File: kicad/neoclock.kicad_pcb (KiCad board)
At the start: 2 copper layers, 28.1 x 42.7 mm, 22 parts, among them CON1 2.1mm 5V, IC1 ATMEGA328P-A, K1 NEOPIXEL, P1 ICSP, SW1 HOUR, SW2 MINUTE, U1 DS1307, X1 16Mhz, X2 32.768kHz

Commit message: updated qfn board
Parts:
- added F1: FUSE, synic:1206_polyfuse, F.Cu at (33.0, 51.3)
- added MH: MountingHole_2-5mm_RevA_Date21Jun2010, Mounting_Holes:MountingHole_2-5mm, F.Cu at (72.6, 56.1)
- added MH: MountingHole_2-5mm_RevA_Date21Jun2010, Mounting_Holes:MountingHole_2-5mm, F.Cu at (42.2, 37.8)
- added MH1: MountingHole_2-5mm_RevA_Date21Jun2010, Mounting_Holes:MountingHole_2-5mm, F.Cu at (72.6, 37.8)
- added TP1: TPGND, synicpretty:TESTPOINT, F.Cu at (73.9, 50.8)
- added TP2: TPVCC, TESTPOINT, F.Cu at (73.9, 47.2)
- C4: footprint Capacitors_SMD:c_elec_3x5.3 -> Capacitors_SMD:c_elec_4x5.3
- CON1: footprint synic:BARREL_JACK_SMD -> BARREL_JACK_SMD
- IC1: value ATMEGA328P-A -> ATMEGA328P-MM; footprint SMD_Packages:TQFP32 -> SMD_Packages:QFN28
- PHOTOR1: footprint synic:PHOTORESISTOR -> PHOTORESISTOR
- SW1: value HOUR -> H
- SW2: value MINUTE -> M
- moved U1 45.8 mm to (59.9, 47.0)
- moved X2 43.2 mm to (67.1, 47.8)
- moved C5 40.7 mm to (52.1, 56.9), turned to 270 degrees
- moved PHOTOR1 38.6 mm to (66.5, 36.8)
- moved R3 38.2 mm to (59.9, 38.4), turned to 90 degrees
- moved R2 37.5 mm to (57.7, 38.4), turned to 90 degrees
- moved BT1 36.9 mm to (62.7, 46.0), turned to 0 degrees
- moved C6 36.8 mm to (54.4, 56.9), turned to 270 degrees
- moved X1 36.8 mm to (53.3, 52.8), turned to 0 degrees
- moved C7 34.6 mm to (52.6, 46.5), turned to 90 degrees
- moved C2 26.5 mm to (53.6, 49.5), turned to 180 degrees
- moved R1 26.2 mm to (55.4, 38.4), turned to 90 degrees
- moved SW2 23.4 mm to (66.8, 54.6)
- moved SW1 23.2 mm to (60.2, 54.6)
- moved IC1 20.4 mm to (46.5, 47.2)
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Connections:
- CON1 pad 1: VCC -> Net-(CON1-Pad1)
- IC1 pad 16: Net-(IC1-Pad16) -> VCC
- IC1 pad 17: Net-(IC1-Pad17) -> Net-(C2-Pad1)
- IC1 pad 18: VCC -> GND
- IC1 pad 20: Net-(C2-Pad1) -> Net-(IC1-Pad20)
- IC1 pad 21: GND -> Net-(IC1-Pad21)
- IC1 pad 23: Net-(IC1-Pad23) -> I2CSDA
- IC1 pad 24: Net-(IC1-Pad24) -> I2CSCL
- IC1 pad 27: I2CSDA -> Net-(IC1-Pad27)
- IC1 pad 28: I2CSCL -> Net-(IC1-Pad28)
- IC1 pad 29: Net-(IC1-Pad29) -> GND
- IC1 pad 3: GND -> VCC
- IC1 pad 4: VCC -> GND
- IC1 pad 5: GND -> Net-(C5-Pad2)
- IC1 pad 6: VCC -> Net-(C6-Pad2)
- IC1 pad 7: Net-(C5-Pad2) -> Net-(IC1-Pad7)
- IC1 pad 8: Net-(C6-Pad2) -> Net-(IC1-Pad8)
- K1 pad 3: Net-(IC1-Pad10) -> Net-(IC1-Pad8)
- P1 pad 1: Net-(IC1-Pad16) -> Net-(IC1-Pad14)
- P1 pad 3: Net-(IC1-Pad17) -> Net-(IC1-Pad15)
- P1 pad 4: Net-(IC1-Pad15) -> Net-(IC1-Pad13)
- P1 pad 5: Net-(IC1-Pad29) -> Net-(IC1-Pad25)
- PHOTOR1 pad 2: Net-(IC1-Pad26) -> Net-(IC1-Pad22)
- R2 pad 2: Net-(IC1-Pad29) -> Net-(IC1-Pad25)
- R3 pad 1: Net-(IC1-Pad26) -> Net-(IC1-Pad22)
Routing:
- net GND: track 0.00 -> 139.1 mm, vias 0 -> 3
- net Net-(IC1-Pad15): track 0.00 -> 60.2 mm, vias 0 -> 1
- net Net-(IC1-Pad25): track 0.00 -> 60.0 mm, vias 0 -> 3
- net Net-(IC1-Pad1): track 0.00 -> 35.4 mm, vias 0 -> 2
- net Net-(IC1-Pad14): track 0.00 -> 29.8 mm, vias 0 -> 1
- net Net-(C6-Pad2): track 0.00 -> 29.2 mm
- net VCC: track 83.6 -> 112.7 mm, vias 2 -> 1
- net Net-(IC1-Pad2): track 0.00 -> 27.7 mm, vias 0 -> 2
- net Net-(BT1-Pad1): track 0.00 -> 26.4 mm, vias 0 -> 1
- net Net-(IC1-Pad22): track 0.00 -> 25.7 mm, vias 0 -> 2
- net Net-(C5-Pad2): track 0.00 -> 25.5 mm
- net Net-(IC1-Pad8): track 0.00 -> 24.6 mm, vias 0 -> 1
- net Net-(IC1-Pad13): track 0.00 -> 23.2 mm, vias 0 -> 1
- net I2CSCL: track 0.00 -> 19.5 mm
- net Net-(CON1-Pad1): track 0.00 -> 13.8 mm
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- added copper zone on B.Cu, net GND
- added copper zone on F.Cu, net GND
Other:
- board size 28.1 x 42.7 mm -> 51.3 x 23.9 mm
- net class POWER removed
- net class PWR added: clearance 0.254, trace_width 0.35, via_dia 0.889, via_drill 0.635
- rule trace_min: 0.254 -> 0.17
- board text added: "NeoClock v5 arolsen@gmail.com"
- board text removed: "+"

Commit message: commit latest changes for orsonz
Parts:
- removed C3: 100uF, Capacitors_SMD:c_elec_5x5.3
- added R4: 4.7k, Resistors_SMD:Resistor_SMD0805_ReflowWave, F.Cu at (52.1, 54.6)
- added R5: 4.7k, Resistors_SMD:Resistor_SMD0805_ReflowWave, F.Cu at (47.8, 54.6)
- C4: footprint Capacitors_SMD:c_elec_4x5.3 -> Capacitors_Tantalum_SMD:TantalC_SizeA_EIA-3216_Reflow
- C5, C6, X1: moved to B.Cu
- R1, R2, R3: footprint Resistors_SMD:Resistor_SMD0805_HandSoldering -> Resistors_SMD:Resistor_SMD0805_ReflowWave
- SW1: value H -> HOUR
- SW2: value M -> MINUTE
- moved C6 26.5 mm to (37.3, 36.6), turned to 0 degrees
- moved C5 22.0 mm to (43.7, 36.6), turned to 180 degrees
- moved MH 18.3 mm to (41.9, 56.1)
- moved P1 18.0 mm to (28.4, 38.1), turned to 180 degrees
- moved X1 17.1 mm to (40.4, 41.7), turned to 180 degrees
- moved C4 16.4 mm to (40.1, 39.4), turned to 0 degrees
- moved C2 13.5 mm to (40.1, 49.5), turned to 90 degrees
- moved CON1 11.7 mm to (29.2, 51.6), turned to 0 degrees
- moved F1 10.5 mm to (35.8, 41.1), turned to 270 degrees
- moved C7 9.32 mm to (61.7, 48.3), turned to 0 degrees
- moved D1 5.24 mm to (66.3, 41.4), turned to 0 degrees
- moved U1 4.34 mm to (55.9, 45.5), turned to 180 degrees
- moved R2 4.10 mm to (53.6, 37.8)
- moved R3 3.84 mm to (56.1, 37.8)
- moved R1 3.34 mm to (58.7, 37.8)
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- renumbered MH to MH5
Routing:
- net GND: track 139.1 -> 0.00 mm, vias 3 -> 0
- net VCC: track 112.7 -> 0.00 mm, vias 1 -> 0
- net Net-(IC1-Pad15): track 60.2 -> 0.00 mm, vias 1 -> 0
- net Net-(IC1-Pad25): track 60.0 -> 0.00 mm, vias 3 -> 0
- net Net-(IC1-Pad1): track 35.4 -> 0.00 mm, vias 2 -> 0
- net Net-(IC1-Pad14): track 29.8 -> 0.00 mm, vias 1 -> 0
- net Net-(C6-Pad2): track 29.2 -> 0.00 mm
- net Net-(IC1-Pad2): track 27.7 -> 0.00 mm, vias 2 -> 0
- net Net-(BT1-Pad1): track 26.4 -> 0.00 mm, vias 1 -> 0
- net Net-(IC1-Pad22): track 25.7 -> 0.00 mm, vias 2 -> 0
- net Net-(C5-Pad2): track 25.5 -> 0.00 mm
- net Net-(IC1-Pad8): track 24.6 -> 0.00 mm, vias 1 -> 0
- net Net-(IC1-Pad13): track 23.2 -> 0.00 mm, vias 1 -> 0
- net I2CSCL: track 19.5 -> 0.00 mm
- net Net-(CON1-Pad1): track 13.8 -> 0.00 mm
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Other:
- net class LRGPWR added: clearance 0.254, trace_width 0.4, via_dia 0.889, via_drill 0.635

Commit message: woot
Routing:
- net GND: track 0.00 -> 150.0 mm, vias 0 -> 12
- net VCC: track 0.00 -> 148.2 mm
- net Net-(IC1-Pad22): track 0.00 -> 66.4 mm, vias 0 -> 2
- net Net-(IC1-Pad25): track 0.00 -> 50.0 mm, vias 0 -> 2
- net Net-(IC1-Pad15): track 0.00 -> 35.1 mm, vias 0 -> 1
- net Net-(IC1-Pad13): track 0.00 -> 26.6 mm, vias 0 -> 1
- net Net-(IC1-Pad1): track 0.00 -> 26.6 mm, vias 0 -> 2
- net Net-(BT1-Pad1): track 0.00 -> 24.1 mm, vias 0 -> 1
- net Net-(IC1-Pad2): track 0.00 -> 23.6 mm, vias 0 -> 2
- net Net-(IC1-Pad14): track 0.00 -> 21.4 mm, vias 0 -> 1
- net Net-(D1-Pad1): track 0.00 -> 17.8 mm, vias 0 -> 2
- net I2CSCL: track 0.00 -> 17.2 mm
- net Net-(C6-Pad2): track 0.00 -> 15.7 mm, vias 0 -> 1
- net Net-(U1-Pad1): track 0.00 -> 15.2 mm, vias 0 -> 2
- net I2CSDA: track 0.00 -> 13.7 mm, vias 0 -> 2
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
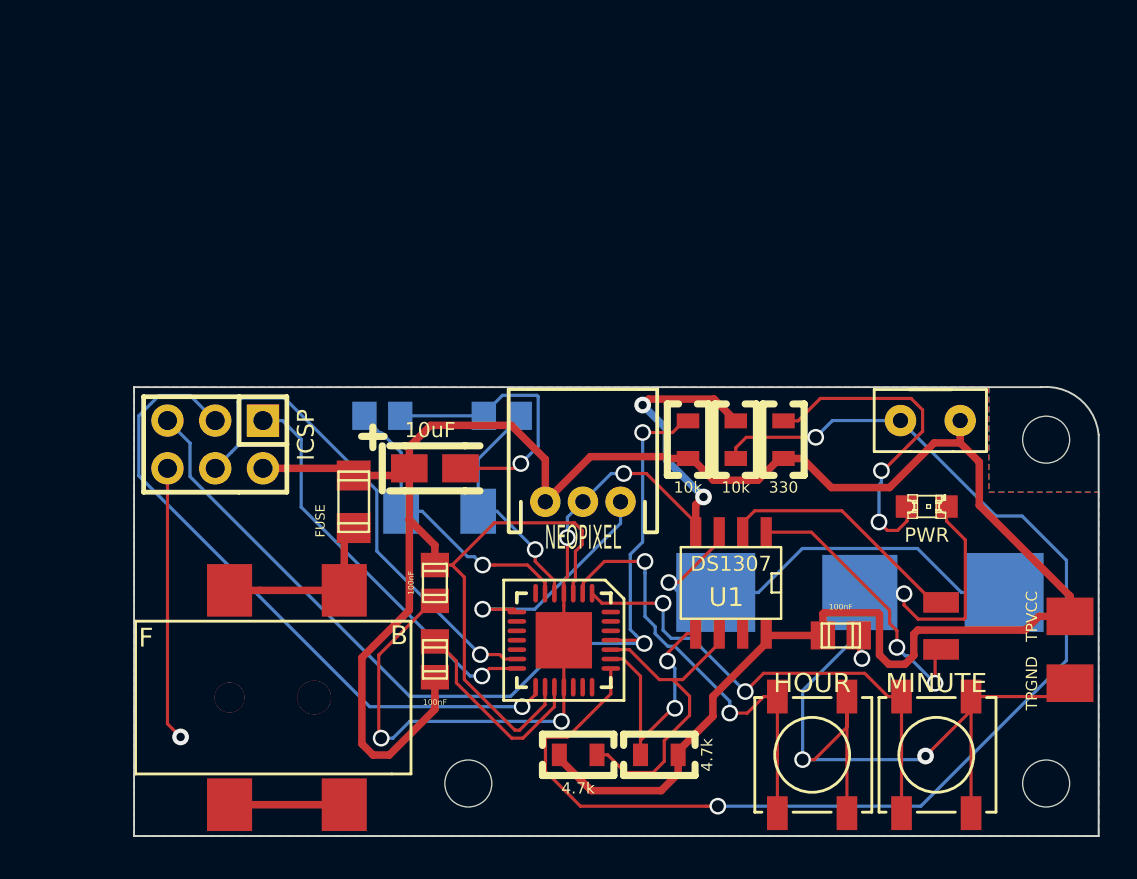
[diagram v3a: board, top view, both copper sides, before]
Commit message: add ftdi headers
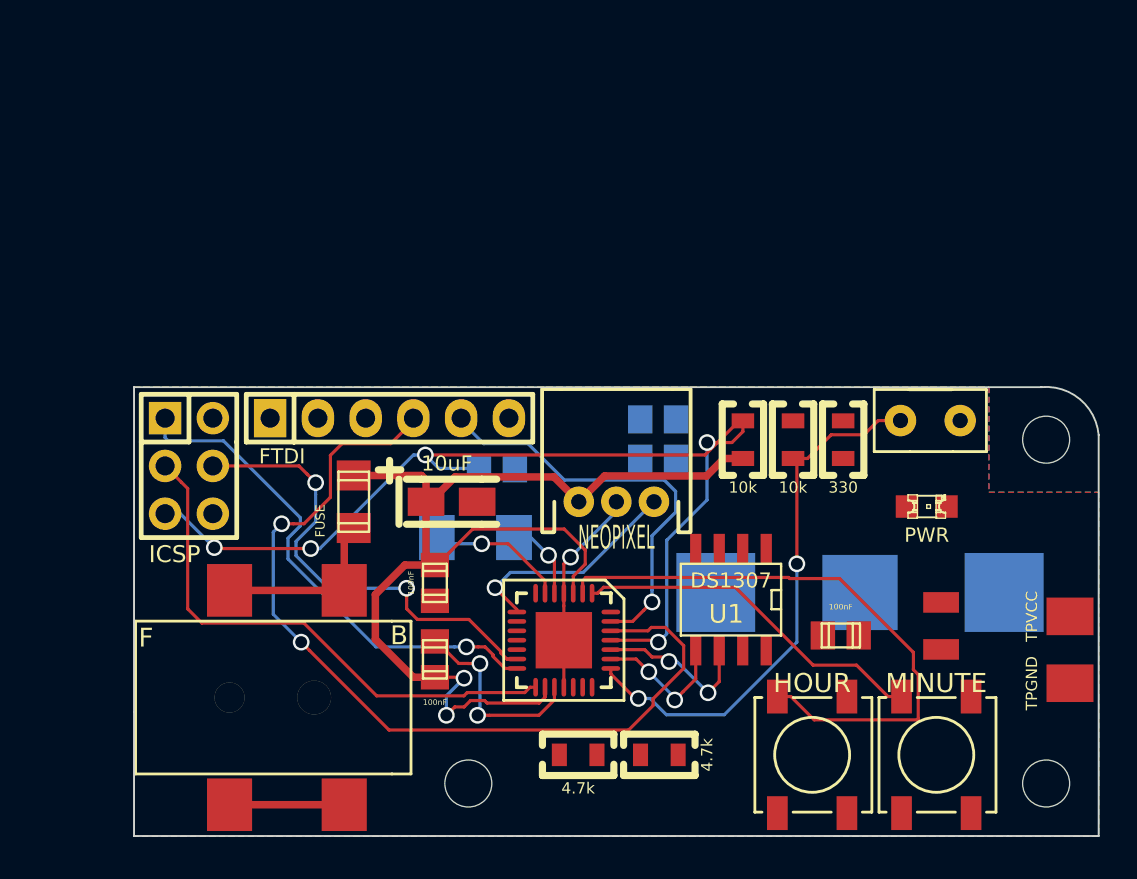
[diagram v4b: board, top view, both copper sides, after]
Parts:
- added C3: 100nF, Capacitors_SMD:c_0805, B.Cu at (43.4, 39.4)
- added P2: FTDI, Pin_Headers:Pin_Header_Straight_1x06, F.Cu at (37.7, 36.7)
- moved C6 14.7 mm to (52.0, 36.8)
- moved C5 8.63 mm to (52.0, 38.9), turned to 0 degrees
- moved R1 3.17 mm to (61.8, 37.8)
- moved R3 3.05 mm to (59.2, 37.8)
- moved R2 2.92 mm to (56.5, 37.8)
- moved X1 2.36 mm to (42.3, 43.1)
- moved C4 1.99 mm to (41.0, 41.1)
- moved P1 1.81 mm to (27.1, 39.2), turned to 270 degrees
- moved K1 1.78 mm to (49.8, 41.1)
- moved U1 0.89 mm to (55.9, 46.4)
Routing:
- net GND: track 150.0 -> 17.1 mm, vias 12 -> 1
- net VCC: track 148.2 -> 59.8 mm, vias 0 -> 2
- net Net-(IC1-Pad26): track 0.00 -> 47.2 mm, vias 0 -> 2
- net Net-(IC1-Pad22): track 66.4 -> 29.1 mm
- net Net-(BT1-Pad1): track 24.1 -> 0.00 mm, vias 1 -> 0
- net Net-(IC1-Pad27): track 0.00 -> 22.1 mm, vias 0 -> 1
- net Net-(D1-Pad1): track 17.8 -> 0.00 mm, vias 2 -> 0
- net Net-(U1-Pad1): track 15.2 -> 0.00 mm, vias 2 -> 0
- net Net-(U1-Pad2): track 13.3 -> 0.00 mm
- net I2CSCL: track 17.2 -> 8.62 mm, vias 0 -> 2
- net Net-(C6-Pad2): track 15.7 -> 7.37 mm
- net Net-(C5-Pad2): track 12.6 -> 4.38 mm
- net Net-(IC1-Pad2): track 23.6 -> 31.6 mm, vias 2 -> 0
- net Net-(IC1-Pad1): track 26.6 -> 19.0 mm, vias 2 -> 0
- net Net-(IC1-Pad15): track 35.1 -> 28.7 mm, vias 1 -> 0
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
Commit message: woot
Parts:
- C2, C7, U1, X2: moved to B.Cu
- moved X2 21.8 mm to (47.0, 56.5), turned to 0 degrees
- moved R5 11.7 mm to (55.2, 45.6), turned to 270 degrees
- moved U1 9.21 mm to (52.1, 54.8)
- moved R4 9.00 mm to (52.5, 45.6), turned to 270 degrees
- moved C7 8.64 mm to (56.0, 54.7), turned to 270 degrees
- moved C2 8.48 mm to (47.2, 54.2), turned to 0 degrees
- moved C1 6.05 mm to (40.0, 51.5)
- moved IC1 1.09 mm to (46.0, 48.9)
- moved MH 0.30 mm to (42.2, 56.1)
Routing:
- net Net-(BT1-Pad1): track 0.00 -> 30.8 mm, vias 0 -> 2
- net Net-(IC1-Pad22): track 29.1 -> 0.00 mm, vias 2 -> 0
- net Net-(IC1-Pad26): track 47.2 -> 20.2 mm
- net Net-(C3-Pad1): track 54.4 -> 35.7 mm, vias 5 -> 0
- net GND: track 17.1 -> 30.9 mm, vias 1 -> 2
- net Net-(C6-Pad2): track 7.37 -> 20.8 mm
- net Net-(IC1-Pad8): track 12.1 -> 0.00 mm, vias 1 -> 0
- net Net-(IC1-Pad1): track 19.0 -> 30.5 mm, vias 0 -> 2
- net Net-(C2-Pad1): track 10.8 -> 0.00 mm, vias 2 -> 0
- net Net-(C5-Pad2): track 4.38 -> 14.6 mm
- net Net-(U1-Pad1): track 0.00 -> 9.62 mm
- net I2CSDA: track 7.48 -> 16.3 mm, vias 2 -> 1
- net Net-(U1-Pad2): track 0.00 -> 8.83 mm
- net Net-(IC1-Pad14): track 27.1 -> 34.6 mm
- net Net-(IC1-Pad27): track 22.1 -> 29.5 mm
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- added copper zone on F.Cu, net VCC

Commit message: saving
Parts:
- SW1: value HOUR -> H
- SW2: value MINUTE -> M
- moved K1 19.8 mm to (30.1, 39.0), turned to 90 degrees
- moved C6 13.6 mm to (40.3, 43.7), turned to 180 degrees
- moved P2 12.2 mm to (49.9, 36.6)
- moved C3 11.9 mm to (55.3, 40.3), turned to 0 degrees
- moved P1 11.2 mm to (38.2, 37.8), turned to 180 degrees
- moved R1 3.58 mm to (62.3, 41.4), turned to 0 degrees
- moved X1 3.33 mm to (45.6, 43.1)
- moved R3 2.91 mm to (62.0, 37.2)
- moved R2 2.68 mm to (59.1, 37.3)
- moved C4 2.07 mm to (41.8, 43.1)
- moved C5 1.68 mm to (51.2, 40.3), turned to 180 degrees
- moved F1 1.50 mm to (35.1, 42.5), turned to 0 degrees
- moved C1 0.86 mm to (40.9, 51.5)
- moved MH 0.34 mm to (41.9, 56.3)
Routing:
- net VCC: track 58.3 -> 0.00 mm, vias 2 -> 0
- net Net-(C3-Pad1): track 35.7 -> 0.00 mm
- net Net-(IC1-Pad14): track 34.6 -> 0.00 mm, vias 1 -> 0
- net Net-(IC1-Pad15): track 32.3 -> 0.00 mm
- net GND: track 30.9 -> 0.00 mm, vias 2 -> 0
- net Net-(BT1-Pad1): track 30.8 -> 0.00 mm, vias 2 -> 0
- net Net-(IC1-Pad1): track 30.5 -> 0.00 mm, vias 2 -> 0
- net Net-(IC1-Pad27): track 29.5 -> 0.00 mm, vias 1 -> 0
- net Net-(IC1-Pad2): track 25.5 -> 0.00 mm
- net Net-(C6-Pad2): track 20.8 -> 0.00 mm, vias 1 -> 0
- net Net-(IC1-Pad26): track 20.2 -> 0.00 mm, vias 2 -> 0
- net Net-(IC1-Pad13): track 19.6 -> 0.00 mm, vias 1 -> 0
- net I2CSDA: track 16.3 -> 0.00 mm, vias 1 -> 0
- net Net-(C5-Pad2): track 14.6 -> 0.00 mm, vias 1 -> 0
- net I2CSCL: track 11.3 -> 0.00 mm, vias 1 -> 0
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- added copper zone on B.Cu, net VCC

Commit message: all routed
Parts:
- moved C3 0.20 mm to (55.1, 40.3)
- turned F1 to 180 degrees
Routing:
- net VCC: track 0.00 -> 157.0 mm, vias 0 -> 7
- net GND: track 0.00 -> 150.3 mm, vias 0 -> 7
- net Net-(BT1-Pad1): track 0.00 -> 55.4 mm
- net Net-(C3-Pad1): track 0.00 -> 48.6 mm, vias 0 -> 2
- net Net-(IC1-Pad15): track 0.00 -> 42.2 mm, vias 0 -> 2
- net Net-(IC1-Pad22): track 0.00 -> 41.7 mm
- net Net-(IC1-Pad13): track 0.00 -> 34.0 mm, vias 0 -> 1
- net Net-(IC1-Pad27): track 0.00 -> 32.9 mm
- net Net-(IC1-Pad1): track 0.00 -> 28.3 mm, vias 0 -> 4
- net Net-(IC1-Pad2): track 0.00 -> 28.2 mm, vias 0 -> 2
- net Net-(IC1-Pad26): track 0.00 -> 20.0 mm, vias 0 -> 1
- net Net-(IC1-Pad14): track 0.00 -> 20.0 mm, vias 0 -> 1
- net Net-(IC1-Pad8): track 0.00 -> 18.2 mm, vias 0 -> 1
- net I2CSCL: track 0.00 -> 12.1 mm, vias 0 -> 2
- net I2CSDA: track 0.00 -> 11.9 mm, vias 0 -> 2
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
